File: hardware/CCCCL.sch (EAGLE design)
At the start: 28 parts, among them IC1 7805L, J1 AVR_SPI_PRG_6NS, U1 LMV324

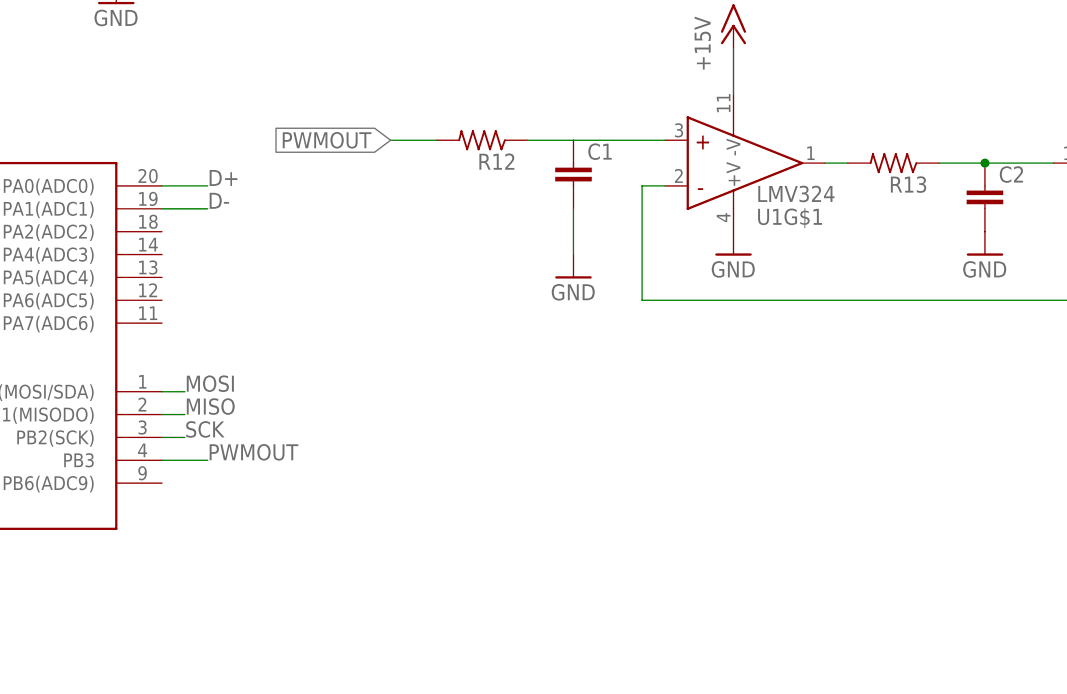
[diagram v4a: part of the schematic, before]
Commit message: added SPI eeprom for data storage
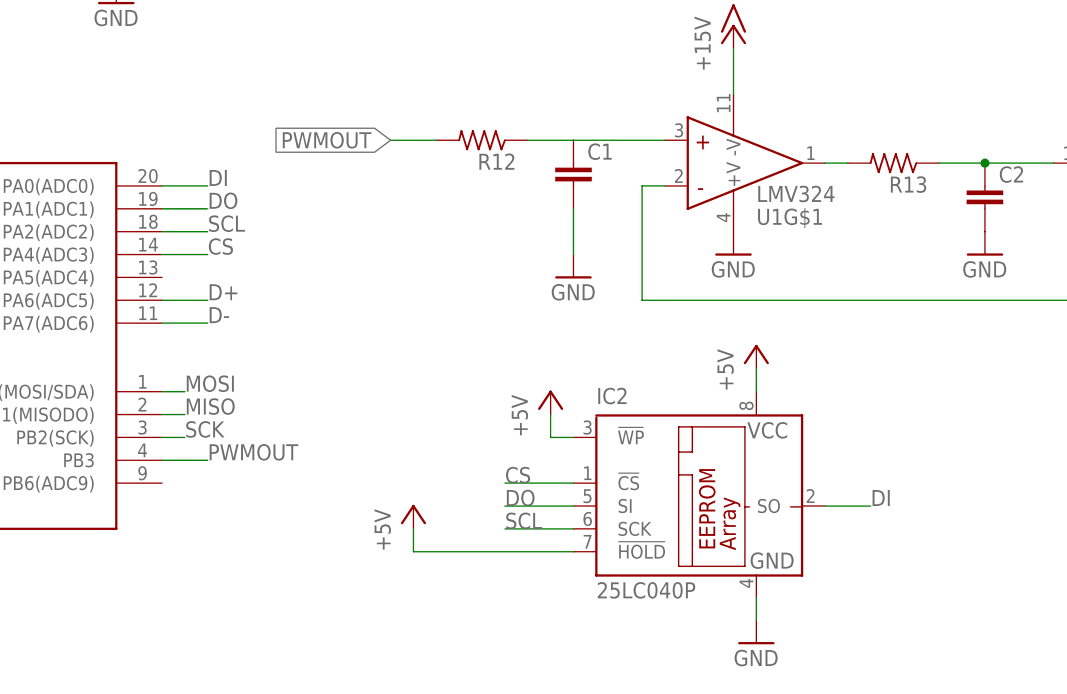
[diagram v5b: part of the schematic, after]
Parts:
- added IC2: 25LC040P, microchip:25LC040P
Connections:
- new net CS: IC2.!CS, U$1.PA4(ADC3)
- new net DI: IC2.SO, U$1.PA0(ADC0)
- new net DO: IC2.SI, U$1.PA1(ADC1)
- new net SCL: IC2.SCK, U$1.PA2(ADC2)
- net +5V: now also IC2.!HOLD, IC2.!WP, IC2.VCC
- net D+: now also U$1.PA6(ADC5); no longer U$1.PA0(ADC0)
- net D-: now also U$1.PA7(ADC6); no longer U$1.PA1(ADC1)
- net GND: now also IC2.GND
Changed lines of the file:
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@@
 <part name="R16" library="resistor" deviceset="R-US_" device="0309/12"/>
 <part name="P+6" library="supply1" deviceset="+5V" device=""/>
+<part name="IC2" library="microchip" deviceset="25*" device="P" technology="LC040"/>
+<part name="P+7" library="supply1" deviceset="+5V" device=""/>
+<part name="GND11" library="supply1" deviceset="GND" device=""/>
+<part name="P+8" library="supply1" deviceset="+5V" device=""/>
+<part name="P+9" library="supply1" deviceset="+5V" device=""/>
 </parts>
 <sheets>
@@
 <instance part="R16" gate="G$1" x="96.52" y="93.98" rot="R90"/>
 <instance part="P+6" gate="1" x="96.52" y="104.14"/>
+<instance part="IC2" gate="G$1" x="30.48" y="20.32"/>
+<instance part="P+7" gate="1" x="38.1" y="38.1"/>
+<instance part="GND11" gate="1" x="38.1" y="5.08"/>
+<instance part="P+8" gate="1" x="0" y="20.32"/>
+<instance part="P+9" gate="1" x="15.24" y="33.02"/>
 </instances>
 <busses>
@@
 <pinref part="GND10" gate="1" pin="GND"/>
 </segment>
+<segment>
+<pinref part="IC2" gate="G$1" pin="GND"/>
+<wire x1="38.1" y1="10.16" x2="38.1" y2="7.62" width="0.1524" layer="91"/>
+<pinref part="GND11" gate="1" pin="GND"/>
+</segment>
 </net>
 <net name="VB" class="0">
@@
 <pinref part="P+6" gate="1" pin="+5V"/>
 </segment>
+<segment>
+<pinref part="P+7" gate="1" pin="+5V"/>
+<pinref part="IC2" gate="G$1" pin="VCC"/>
+<wire x1="38.1" y1="35.56" x2="38.1" y2="33.02" width="0.1524" layer="91"/>
+</segment>
+<segment>
+<pinref part="P+8" gate="1" pin="+5V"/>
+<wire x1="0" y1="17.78" x2="0" y2="15.24" width="0.1524" layer="91"/>
+<pinref part="IC2" gate="G$1" pin="!HOLD"/>
+<wire x1="0" y1="15.24" x2="17.78" y2="15.24" width="0.1524" layer="91"/>
+</segment>
+<segment>
+<pinref part="IC2" gate="G$1" pin="!WP"/>
+<pinref part="P+9" gate="1" pin="+5V"/>
+<wire x1="17.78" y1="27.94" x2="15.24" y2="27.94" width="0.1524" layer="91"/>
+<wire x1="15.24" y1="27.94" x2="15.24" y2="30.48" width="0.1524" layer="91"/>
+</segment>
 </net>
 <net name="MISO" class="0">
@@
 </segment>
 <segment>
-<pinref part="U$1" gate="G$1" pin="PA1(ADC1)"/>
-<wire x1="-27.94" y1="53.34" x2="-22.86" y2="53.34" width="0.1524" layer="91"/>
-<label x="-22.86" y="53.34" size="1.778" layer="95"/>
+<pinref part="U$1" gate="G$1" pin="PA7(ADC6)"/>
+<wire x1="-27.94" y1="40.64" x2="-22.86" y2="40.64" width="0.1524" layer="91"/>
+<label x="-22.86" y="40.64" size="1.778" layer="95"/>
 </segment>
 </net>
@@
 </segment>
 <segment>
+<pinref part="U$1" gate="G$1" pin="PA6(ADC5)"/>
+<wire x1="-27.94" y1="43.18" x2="-22.86" y2="43.18" width="0.1524" layer="91"/>
+<label x="-22.86" y="43.18" size="1.778" layer="95"/>
+</segment>
+</net>
+<net name="CS" class="0">
+<segment>
+<pinref part="IC2" gate="G$1" pin="!CS"/>
+<wire x1="17.78" y1="22.86" x2="10.16" y2="22.86" width="0.1524" layer="91"/>
+<label x="10.16" y="22.86" size="1.778" layer="95"/>
+</segment>
+<segment>
+<pinref part="U$1" gate="G$1" pin="PA4(ADC3)"/>
+<wire x1="-27.94" y1="48.26" x2="-22.86" y2="48.26" width="0.1524" layer="91"/>
+<label x="-22.86" y="48.26" size="1.778" layer="95"/>
+</segment>
+</net>
+<net name="DO" class="0">
+<segment>
+<pinref part="U$1" gate="G$1" pin="PA1(ADC1)"/>
+<wire x1="-27.94" y1="53.34" x2="-22.86" y2="53.34" width="0.1524" layer="91"/>
+<label x="-22.86" y="53.34" size="1.778" layer="95"/>
+</segment>
+<segment>
+<pinref part="IC2" gate="G$1" pin="SI"/>
+<wire x1="17.78" y1="20.32" x2="10.16" y2="20.32" width="0.1524" layer="91"/>
+<label x="10.16" y="20.32" size="1.778" layer="95"/>
+</segment>
+</net>
+<net name="SCL" class="0">
+<segment>
+<pinref part="U$1" gate="G$1" pin="PA2(ADC2)"/>
+<wire x1="-27.94" y1="50.8" x2="-22.86" y2="50.8" width="0.1524" layer="91"/>
+<label x="-22.86" y="50.8" size="1.778" layer="95"/>
+</segment>
+<segment>
+<pinref part="IC2" gate="G$1" pin="SCK"/>
+<wire x1="17.78" y1="17.78" x2="10.16" y2="17.78" width="0.1524" layer="91"/>
+<label x="10.16" y="17.78" size="1.778" layer="95"/>
+</segment>
+</net>
+<net name="DI" class="0">
+<segment>
+<pinref part="IC2" gate="G$1" pin="SO"/>
+<wire x1="45.72" y1="20.32" x2="50.8" y2="20.32" width="0.1524" layer="91"/>
+<label x="50.8" y="20.32" size="1.778" layer="95"/>
+</segment>
+<segment>

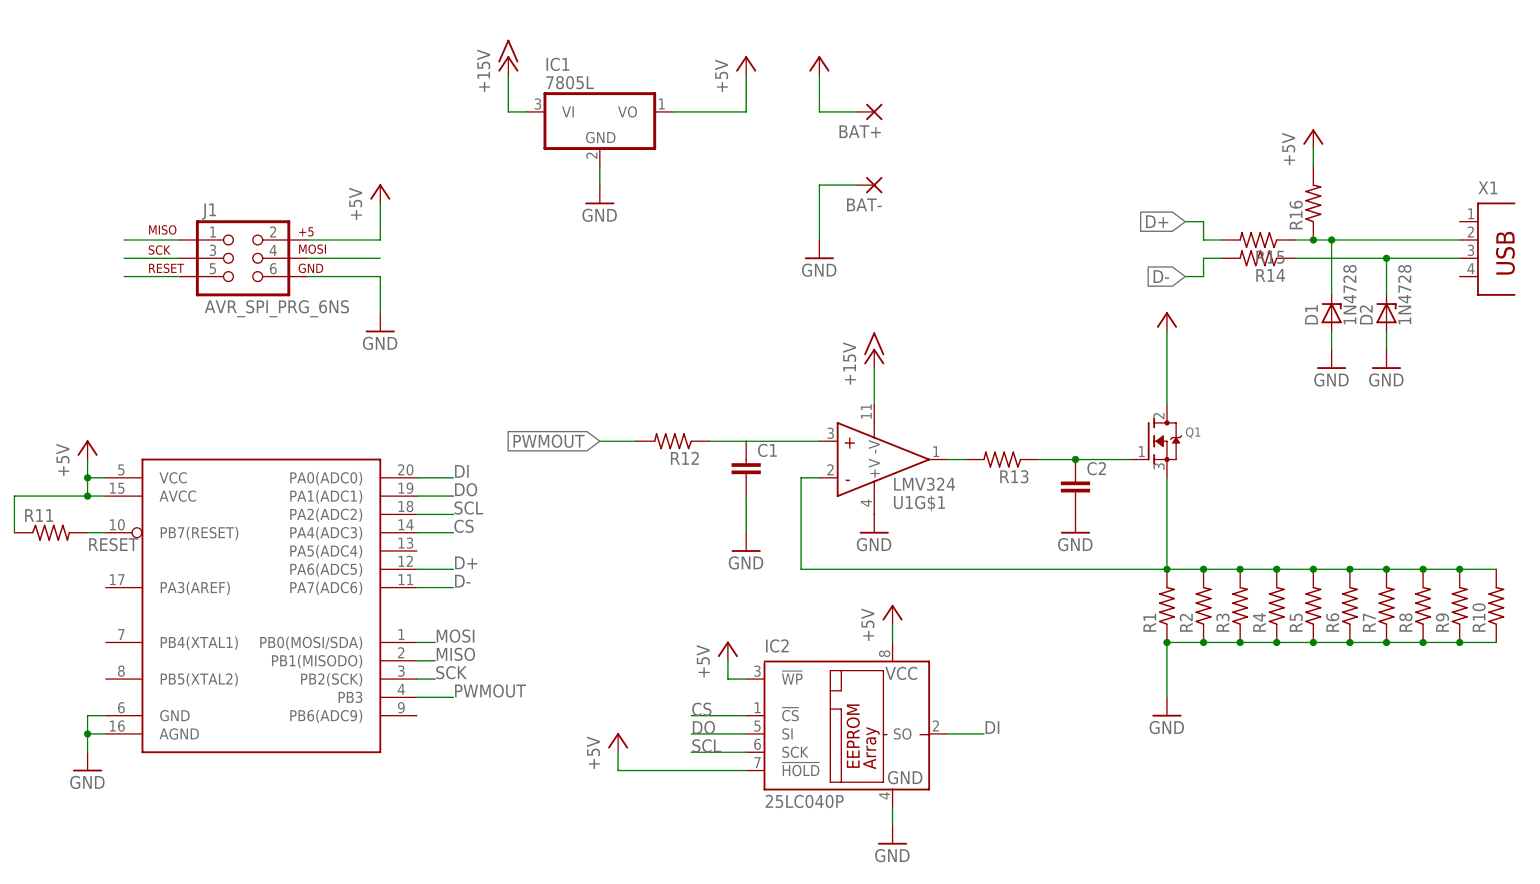
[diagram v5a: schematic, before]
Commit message: Routed board, separated ground planes
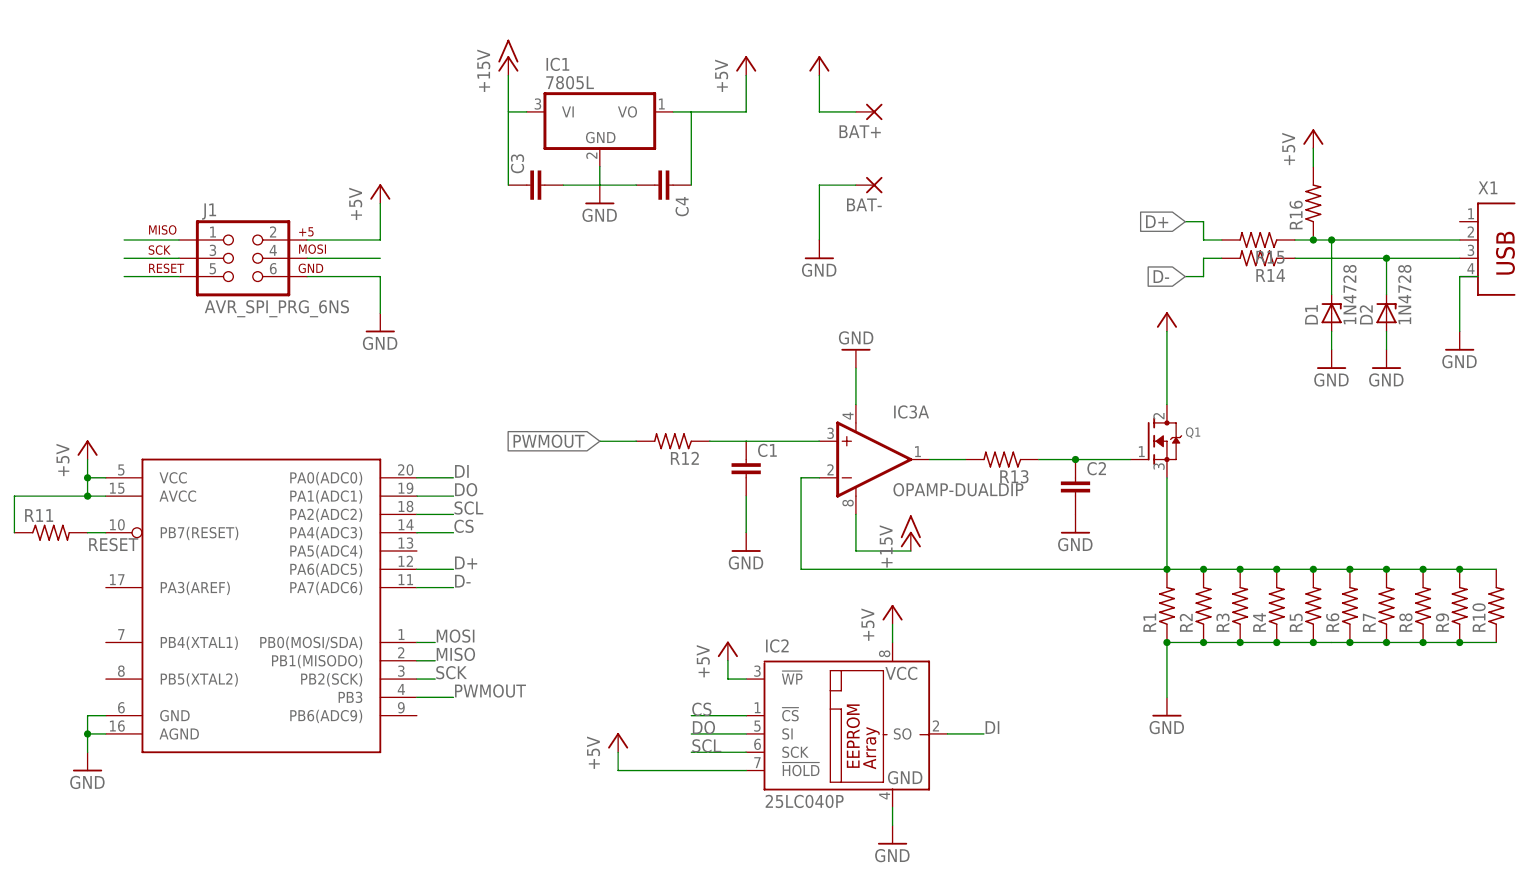
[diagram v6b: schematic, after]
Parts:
- removed U1: LMV324, SparkFun-AnalogIC:LMV324
- added C3, C4: (no value), capacitor-wima:C2,5-3
- added IC3: OPAMP-DUALDIP, SparkFun-AnalogIC:OPAMP-DUALDIP
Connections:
- removed net +3V3: Q1.D
- net +15V: now also C3.1, IC3A.V+; no longer U1G$1.-V
- net +5V: now also C4.1
- net GND: now also C3.2, C4.2, IC3A.V-, X1.4; no longer U1G$1.+V
- net N$1: now also IC3A.OUT; no longer U1G$1.OUT
- net N$2: now also IC3A.-IN; no longer U1G$1.-IN
- net N$4: now also IC3A.+IN; no longer U1G$1.+IN
- net VB: now also Q1.D
